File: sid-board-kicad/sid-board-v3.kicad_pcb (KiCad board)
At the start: 2 copper layers, 36 parts, among them J1 SPI+IRQ+POWER, J2 USB_B_Micro, SW1 SW_EN, SW2 SW_FLASH, U1 SC16IS752IPW, U2 MCP1703A-3302_SOT223, U3 SN65HVD232, U4 SN65HVD232, U5 MCP1703A-5002_SOT223, U6 ESP32-WROOM-32U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

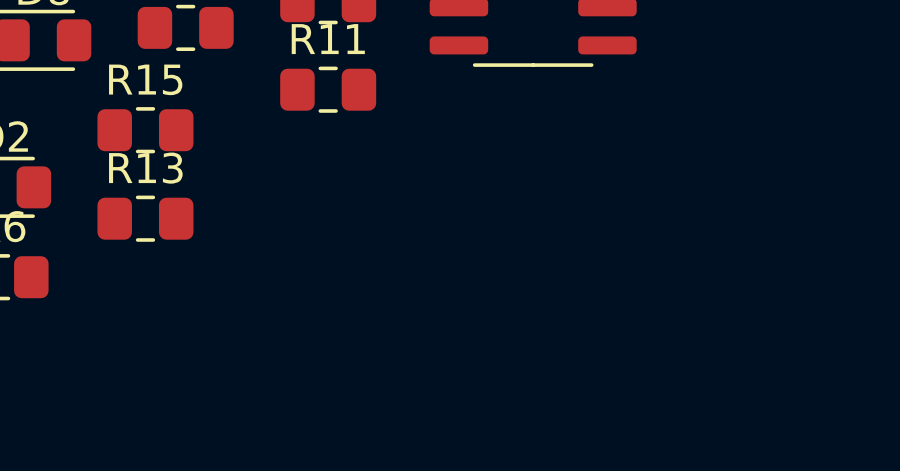
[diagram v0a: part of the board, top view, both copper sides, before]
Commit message: Assigned basic footprints
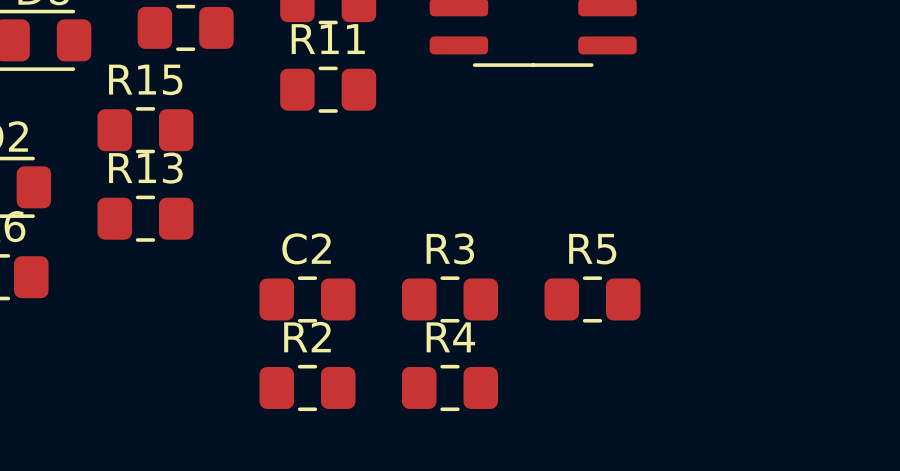
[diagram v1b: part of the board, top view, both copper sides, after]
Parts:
- added C2: 100uF, Capacitor_SMD:C_0805_2012Metric_Pad1.15x1.40mm_HandSolder, F.Cu at (56.5, 45.4)
- added R2: 470, Resistor_SMD:R_0805_2012Metric_Pad1.15x1.40mm_HandSolder, F.Cu at (56.5, 48.4)
- added R3: 470, Resistor_SMD:R_0805_2012Metric_Pad1.15x1.40mm_HandSolder, F.Cu at (61.2, 45.4)
- added R4: 10k, Resistor_SMD:R_0805_2012Metric_Pad1.15x1.40mm_HandSolder, F.Cu at (61.2, 48.4)
- added R5: 10k, Resistor_SMD:R_0805_2012Metric_Pad1.15x1.40mm_HandSolder, F.Cu at (66.0, 45.4)

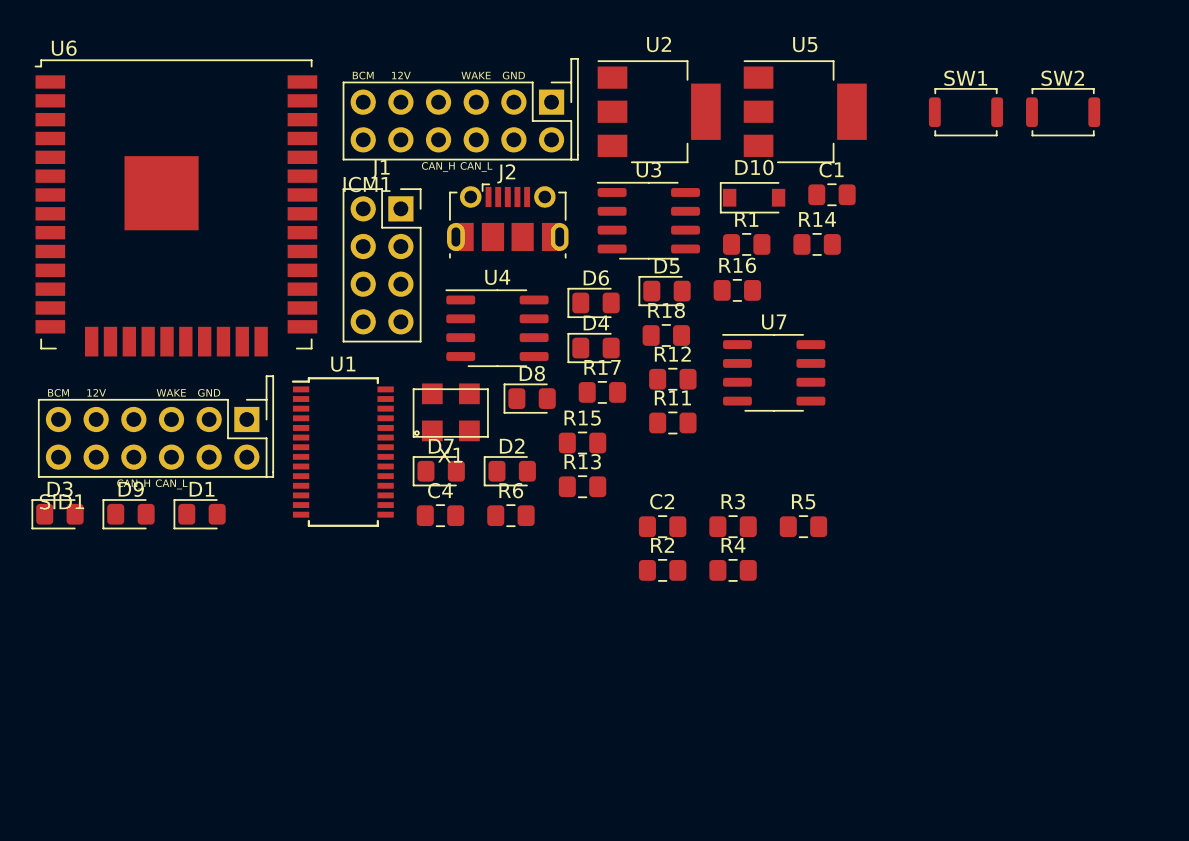
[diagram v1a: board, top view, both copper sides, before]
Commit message: Added UART interface to the SID BOARD V3
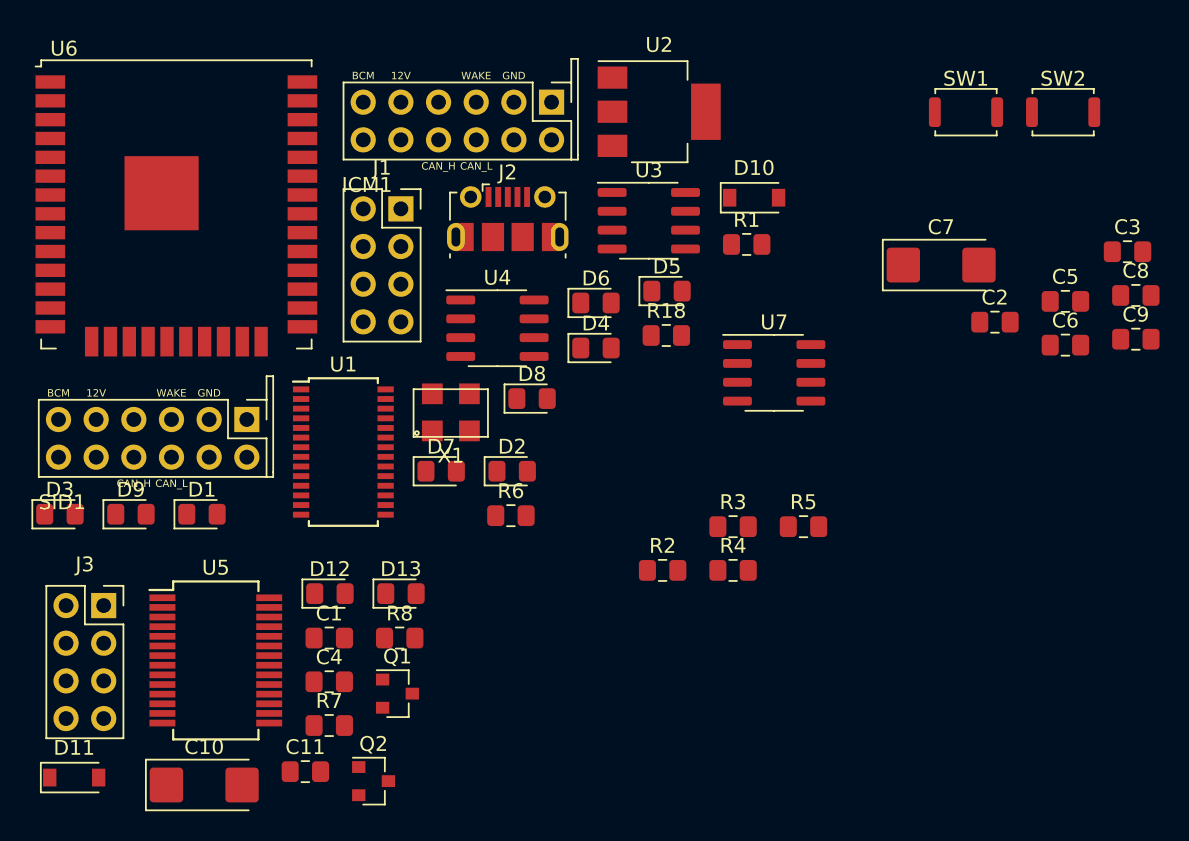
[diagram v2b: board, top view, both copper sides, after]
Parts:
- removed R11, R12, R13, R14, R15, R16, R17: 1K, Resistor_SMD:R_0805_2012Metric_Pad1.15x1.40mm_HandSolder
- added C10: 10uF, Capacitor_Tantalum_SMD:CP_EIA-6032-20_AVX-F_Pad2.25x2.35mm_HandSolder, F.Cu at (25.6, 62.8)
- added C11: 1uF, Capacitor_SMD:C_0805_2012Metric_Pad1.15x1.40mm_HandSolder, F.Cu at (32.4, 61.9)
- added C3: 1uF, Capacitor_SMD:C_0805_2012Metric_Pad1.15x1.40mm_HandSolder, F.Cu at (87.8, 26.9)
- added C5: 1uF, Capacitor_SMD:C_0805_2012Metric_Pad1.15x1.40mm_HandSolder, F.Cu at (83.6, 30.2)
- added C6: 1uF, Capacitor_SMD:C_0805_2012Metric_Pad1.15x1.40mm_HandSolder, F.Cu at (83.6, 33.2)
- added C7: 10uF, Capacitor_Tantalum_SMD:CP_EIA-6032-20_AVX-F_Pad2.25x2.35mm_HandSolder, F.Cu at (75.3, 27.8)
- added C8: 1uF, Capacitor_SMD:C_0805_2012Metric_Pad1.15x1.40mm_HandSolder, F.Cu at (88.4, 29.8)
- added C9: 1uF, Capacitor_SMD:C_0805_2012Metric_Pad1.15x1.40mm_HandSolder, F.Cu at (88.4, 32.8)
- added D11: 1N5819, Diode_SMD:D_SOD-123, F.Cu at (16.8, 62.3)
- added D12: LED0, LED_SMD:LED_0805_2012Metric_Pad1.15x1.40mm_HandSolder, F.Cu at (34.0, 49.9)
- added D13: LED0, LED_SMD:LED_0805_2012Metric_Pad1.15x1.40mm_HandSolder, F.Cu at (38.8, 49.9)
- added J3: UART, Connector_PinSocket_2.54mm:PinSocket_2x04_P2.54mm_Vertical, F.Cu at (18.8, 50.7)
- added Q1: BSS138, Package_TO_SOT_SMD:SOT-23, F.Cu at (38.6, 56.7)
- added Q2: BSS138, Package_TO_SOT_SMD:SOT-23, F.Cu at (37.0, 62.6)
- added R7: 1k, Resistor_SMD:R_0805_2012Metric_Pad1.15x1.40mm_HandSolder, F.Cu at (34.0, 58.8)
- added R8: 1k, Resistor_SMD:R_0805_2012Metric_Pad1.15x1.40mm_HandSolder, F.Cu at (38.8, 52.9)
- C1, C4: value 0.1uF -> 1uF
- C2: value 100uF -> 1uF
- J1: value SPI+IRQ+POWER -> SPI + UART
- R4, R5: value 10k -> 1k
- SW1: value SW_EN -> BOOT
- SW2: value SW_FLASH -> FLASH
- U5: value MCP1703A-5002_SOT223 -> CY7C65213-28PVXI; footprint Package_TO_SOT_SMD:SOT-223-3_TabPin2 -> Package_SO:SSOP-28_5.3x10.2mm_P0.65mm
- moved U5 54.3 mm to (26.4, 54.4)
- moved C1 45.2 mm to (34.0, 52.9)
- moved C2 26.3 mm to (78.9, 31.6)
- moved C4 13.5 mm to (34.0, 55.9)
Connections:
- C1 pad 1: VDD_5V -> VDD_3.3V
- C2 pad 1: GND -> VIN
- C4 pad 1: VDD_3.3V -> Net-(C4-Pad1)
- D1 pad 1: GND -> Net-(D1-Pad1)
- D10 pad 2: Net-(D10-Pad2) -> VBUS
- D2 pad 1: GND -> Net-(D1-Pad1)
- D3 pad 1: GND -> Net-(D1-Pad1)
- D4 pad 1: GND -> Net-(D1-Pad1)
- D5 pad 1: GND -> Net-(D1-Pad1)
- D6 pad 1: GND -> Net-(D1-Pad1)
- D7 pad 1: GND -> Net-(D1-Pad1)
- D8 pad 1: GND -> Net-(D1-Pad1)
- ICM1 pad 1: Net-(ICM1-Pad1) -> (no net)
- ICM1 pad 11: Net-(ICM1-Pad11) -> (no net)
- ICM1 pad 12: Net-(ICM1-Pad12) -> (no net)
- ICM1 pad 4: Net-(ICM1-Pad4) -> (no net)
- ICM1 pad 5: VIN -> Net-(D11-Pad2)
- ICM1 pad 7: Net-(ICM1-Pad7) -> (no net)
- ICM1 pad 8: Net-(ICM1-Pad8) -> (no net)
- J1 pad 1: CLK -> CS
- J1 pad 2: MISO -> CLK
- J1 pad 4: CS -> MISO
- J1 pad 7: VDD_5V -> TXA
- J1 pad 8: IRQ -> RXA
- J2 pad 1: Net-(D10-Pad2) -> VBUS
- J2 pad 2: Net-(J2-Pad2) -> USB_DM
- J2 pad 3: Net-(J2-Pad3) -> USB_DP
- J2 pad 4: Net-(J2-Pad4) -> (no net)
- R18 pad 1: Net-(R18-Pad1) -> Net-(D1-Pad1)
- R18 pad 2: Net-(D8-Pad2) -> GND
- SID1 pad 1: Net-(SID1-Pad1) -> (no net)
- SID1 pad 11: Net-(SID1-Pad11) -> (no net)
- SID1 pad 12: Net-(SID1-Pad12) -> (no net)
- SID1 pad 4: Net-(SID1-Pad4) -> (no net)
- SID1 pad 5: VIN -> Net-(D11-Pad2)
- SID1 pad 7: Net-(SID1-Pad7) -> (no net)
- SID1 pad 8: Net-(SID1-Pad8) -> (no net)
- U1 pad 1: Net-(U1-Pad1) -> (no net)
- U1 pad 16: Net-(U1-Pad16) -> (no net)
- U1 pad 17: Net-(U1-Pad17) -> (no net)
- U1 pad 18: Net-(R18-Pad1) -> Net-(D8-Pad2)
- U1 pad 19: Net-(R17-Pad1) -> Net-(D7-Pad2)
- U1 pad 2: Net-(U1-Pad2) -> (no net)
- U1 pad 20: Net-(R16-Pad1) -> Net-(D6-Pad2)
- U1 pad 21: Net-(R15-Pad1) -> Net-(D5-Pad2)
- U1 pad 25: Net-(R14-Pad1) -> Net-(D4-Pad2)
- U1 pad 26: Net-(R13-Pad1) -> Net-(D3-Pad2)
- U1 pad 27: Net-(R12-Pad1) -> Net-(D2-Pad2)
- U1 pad 28: Net-(R11-Pad1) -> Net-(D1-Pad2)
- U1 pad 7: Net-(U1-Pad7) -> (no net)
- U2 pad 2: GND -> Net-(C2-Pad2)
- U3 pad 5: Net-(U3-Pad5) -> (no net)
- U3 pad 8: Net-(U3-Pad8) -> (no net)
- U4 pad 5: Net-(U4-Pad5) -> (no net)
- U4 pad 8: Net-(U4-Pad8) -> (no net)
- U5 pad 1: VIN -> RX_ESP32
- U5 pad 2: GND -> DTR
- U5 pad 3: VDD_5V -> RTS
- U6 pad 10: Net-(U6-Pad10) -> (no net)
- U6 pad 11: Net-(U6-Pad11) -> (no net)
- U6 pad 12: Net-(U6-Pad12) -> (no net)
- U6 pad 13: Net-(U6-Pad13) -> CLK
- U6 pad 14: Net-(U6-Pad14) -> MISO
- U6 pad 16: Net-(U6-Pad16) -> MOSI
- U6 pad 17: Net-(U6-Pad17) -> (no net)
- U6 pad 18: Net-(U6-Pad18) -> (no net)
- U6 pad 19: Net-(U6-Pad19) -> (no net)
- U6 pad 2: Net-(C2-Pad2) -> VDD_3.3V
- U6 pad 20: Net-(U6-Pad20) -> (no net)
- U6 pad 21: Net-(U6-Pad21) -> (no net)
- U6 pad 22: Net-(U6-Pad22) -> (no net)
- U6 pad 23: Net-(U6-Pad23) -> CS
- U6 pad 27: Net-(U6-Pad27) -> RI
- U6 pad 28: Net-(U6-Pad28) -> SLEEP
- U6 pad 30: Net-(U6-Pad30) -> (no net)
- U6 pad 31: Net-(U6-Pad31) -> (no net)
- U6 pad 32: Net-(U6-Pad32) -> (no net)
- U6 pad 33: Net-(U6-Pad33) -> (no net)
- U6 pad 34: Net-(U6-Pad34) -> RX_ESP32
- U6 pad 35: Net-(U6-Pad35) -> TX_ESP32
- U6 pad 36: Net-(U6-Pad36) -> (no net)
- U6 pad 37: Net-(U6-Pad37) -> (no net)
- U6 pad 4: Net-(U6-Pad4) -> (no net)
- U6 pad 5: Net-(U6-Pad5) -> (no net)
- U6 pad 6: Net-(U6-Pad6) -> (no net)
- U6 pad 7: Net-(U6-Pad7) -> (no net)
- U6 pad 8: Net-(U6-Pad8) -> (no net)
- U6 pad 9: Net-(U6-Pad9) -> (no net)
- U7 pad 5: Net-(U7-Pad5) -> (no net)
- U7 pad 6: CAN_L -> (no net)
- U7 pad 7: CAN_H -> (no net)
- U7 pad 8: Net-(U7-Pad8) -> (no net)

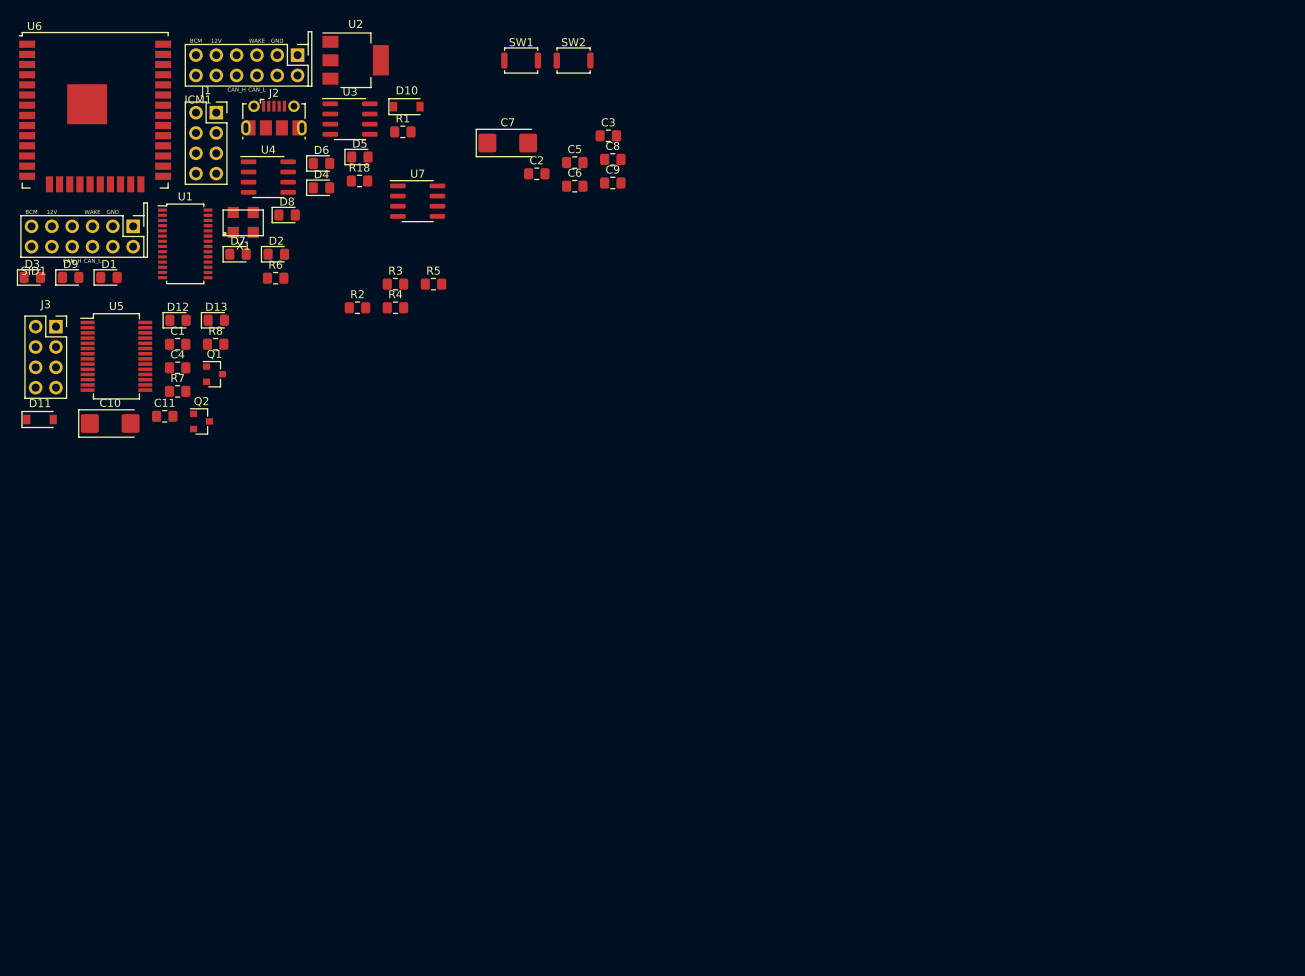
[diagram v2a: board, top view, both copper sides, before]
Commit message: Initial grouped PCB layout
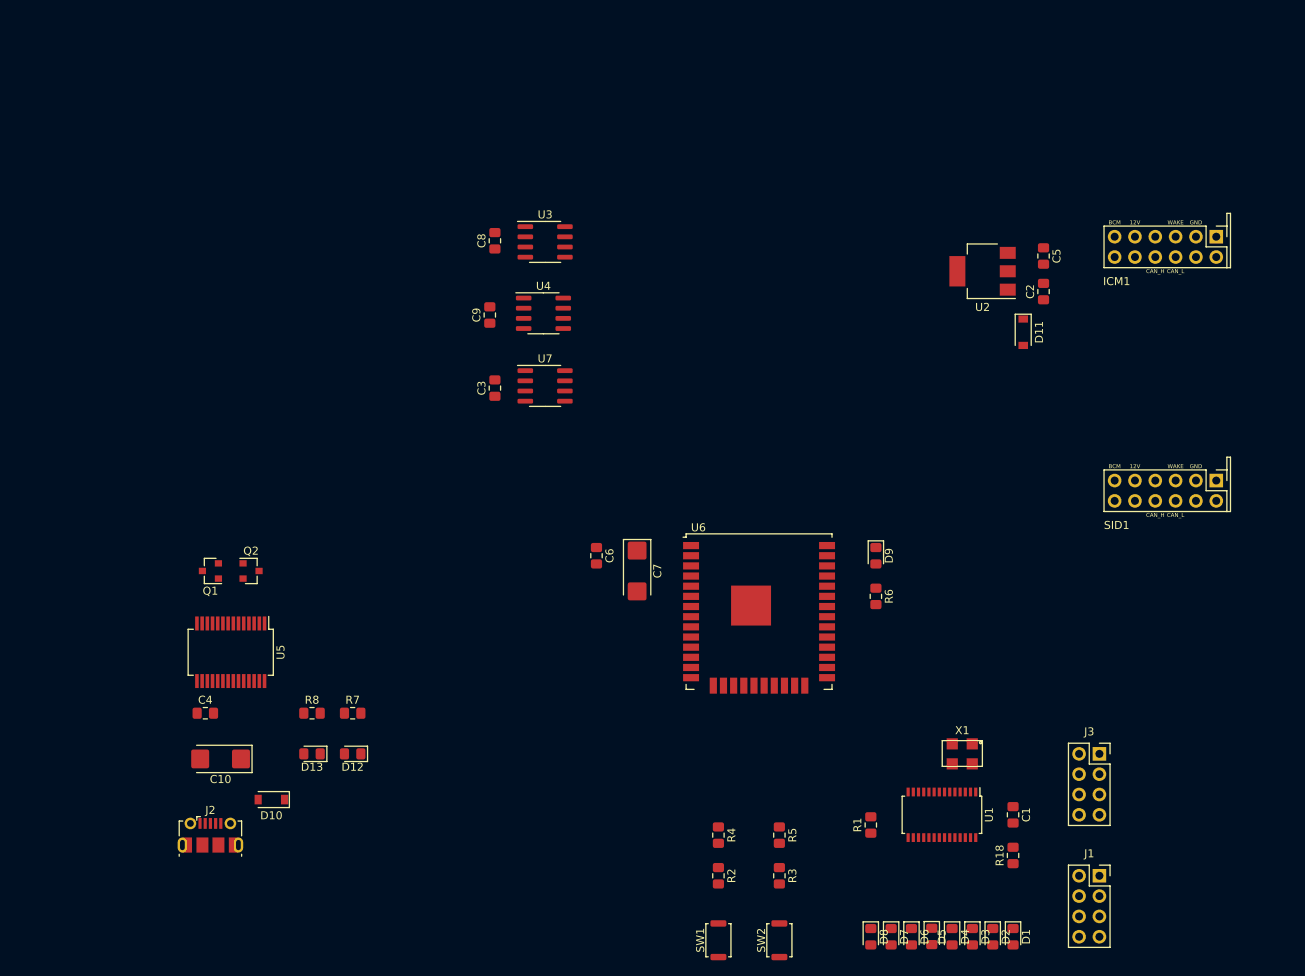
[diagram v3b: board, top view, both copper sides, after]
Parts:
- removed C11: 1uF, Capacitor_SMD:C_0805_2012Metric_Pad1.15x1.40mm_HandSolder
- moved J1 145.9 mm to (149.2, 119.4)
- moved D3 143.5 mm to (133.3, 127.0), turned to 270 degrees
- moved J3 140.9 mm to (149.2, 104.1)
- moved D1 139.9 mm to (138.4, 127.0), turned to 270 degrees
- moved SID1 139.1 mm to (157.5, 71.1)
- moved D2 123.7 mm to (135.9, 127.0), turned to 270 degrees
- moved D11 123.4 mm to (139.7, 51.4), turned to 270 degrees
- moved D4 122.4 mm to (130.8, 127.0), turned to 270 degrees
- moved D6 121.6 mm to (125.7, 127.0), turned to 270 degrees
- moved D5 120.8 mm to (128.3, 127.0), turned to 270 degrees
- moved C1 119.9 mm to (138.4, 111.8), turned to 270 degrees
- moved U1 118.5 mm to (129.5, 111.8), turned to 270 degrees
- moved D7 118.1 mm to (123.2, 127.0), turned to 270 degrees
- moved R18 117.4 mm to (138.4, 116.8), turned to 90 degrees
- moved ICM1 117.1 mm to (157.5, 40.6)
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
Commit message: Experimenting with PCB layouts
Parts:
- removed C10: 10uF, Capacitor_Tantalum_SMD:CP_EIA-6032-20_AVX-F_Pad2.25x2.35mm_HandSolder
- added I-BUS1: Screw_Terminal_01x02, TerminalBlock_Phoenix:TerminalBlock_Phoenix_MKDS-1,5-2-5.08_1x02_P5.08mm_Horizontal, F.Cu at (34.7, 29.5)
- SW1: value BOOT -> SW_EN
- SW2: value FLASH -> SW_FLASH
- moved D1 118.0 mm to (29.0, 82.9), turned to 180 degrees
- moved D2 116.7 mm to (29.0, 80.4), turned to 180 degrees
- moved J3 115.8 mm to (45.7, 52.2)
- moved SID1 115.5 mm to (48.9, 110.5), turned to 180 degrees
- moved D3 115.4 mm to (29.0, 77.9), turned to 180 degrees
- moved D4 114.2 mm to (29.0, 75.3), turned to 180 degrees
- moved D5 113.1 mm to (29.0, 72.8), turned to 180 degrees
- moved D6 112.2 mm to (29.0, 70.2), turned to 180 degrees
- moved D7 111.3 mm to (29.0, 67.7), turned to 180 degrees
- moved J1 111.3 mm to (60.6, 52.1)
- moved R18 110.7 mm to (33.4, 81.9), turned to 0 degrees
- moved D8 110.6 mm to (29.0, 65.2), turned to 180 degrees
- moved ICM1 109.4 mm to (48.9, 27.3)
- moved C1 105.5 mm to (37.2, 81.9), turned to 180 degrees
- moved X1 102.4 mm to (36.4, 67.4)
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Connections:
- U7 pad 6: (no net) -> CAN_L
- U7 pad 7: (no net) -> CAN_H
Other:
- board outline added: 35.4 x 89.2 mm
